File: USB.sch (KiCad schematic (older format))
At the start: 41 parts, among them J6 USB_A, J7 USB_B, U10 USB3320, U11 MIC2025-1YMM, U12 USB3320, U8 xc7z020clg400, Y1 Crystal, Y2 Crystal

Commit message: replacing rescue components foreal
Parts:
- U8: footprint Package_BGA:BGA-400_21.0x21.0mm_Layout20x20_P1.0mm -> DFTcustom:BGA400_0.8p_17mmx17mm
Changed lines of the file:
@@
 F 0 "U8" H 2050 3550 60  0000 L CNN
 F 1 "xc7z020clg400" H 2050 3450 60  0000 L CNN
-F 2 "Package_BGA:BGA-400_21.0x21.0mm_Layout20x20_P1.0mm" H 1850 3300 60  0001 C CNN
+F 2 "DFTcustom:BGA400_0.8p_17mmx17mm" H 1850 3300 60  0001 C CNN
 F 3 "" H 1850 3300 60  0001 C CNN
 	6    1850 3300

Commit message: still works, miraculously
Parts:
- C65, C66, C78, C83, C87: footprint Capacitors_SMD:C_0603 -> Capacitor_SMD:C_0603_1608Metric; symbol DFTBoard-rescue:C_Small- -> Device:C_Small
- C67, C73, C74: footprint Capacitors_SMD:C_1210 -> Capacitor_SMD:C_1210_3225Metric; symbol DFTBoard-rescue:C_Small- -> Device:C_Small
- C68, C70, C71, C72, C77, C79, C81, C82, C86: footprint Capacitors_SMD:C_0603 -> Capacitor_SMD:C_0603_1608Metric; symbol DFTBoard-rescue:C -> Device:C
- C69: footprint Capacitors_SMD:C_0402 -> Capacitor_SMD:C_0402_1005Metric; symbol DFTBoard-rescue:C -> Device:C
- C80: symbol DFTBoard-rescue:C -> Device:C
- R33, R36, R39: symbol DFTBoard-rescue:R -> Device:R
- R35: symbol DFTBoard-rescue:R_Small- -> Device:R_Small
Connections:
- net +1.8V renamed +1V8

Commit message: random updates
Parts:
- removed U8: xc7z020clg400, DFTcustom:BGA400_0.8p_17mmx17mm, symbol DFTBoard-rescue:xc7z020clg400-
- added U20: xc7z020clg484, DFTcustom:BGA-484_19.0x19.0mm_Layout22x22_P0.80mm_dia0.40mm, symbol xilinx7:xc7z020clg484
- C65, C66, C68, C70, C71, C72, C77, C78, C79, C81, C82, C83, C86, C87: footprint Capacitor_SMD:C_0603_1608Metric -> Capacitor_SMD:C_0402_1005Metric
- D3: footprint LEDs:LED_0603 -> Capacitor_SMD:C_0603_1608Metric
- R33, R35, R36, R39: footprint Resistors_SMD:R_0402 -> Resistor_SMD:R_0402_1005Metric
- U10, U12: footprint Microchip:32QFN-3304-5x5B -> Package_DFN_QFN:QFN-32-1EP_5x5mm_P0.5mm_EP3.1x3.1mm
- U11: footprint Crystal:Crystal_HC35-U -> SOP65P490X110-8N:SOP65P490X110-8N
- Y1, Y2: value Crystal -> ABM3-24.000MHZ-D2Y-T; footprint Crystal:Crystal_HC35-U -> ABM3-12.000MHZ-B2-T:XTAL500X320X130N
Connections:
- net +1V8: no longer C65.1, C66.1, C67.1, R33.2
- net +3V3: now also C65.1, C66.1, C67.1, R33.2, U20.A10 (VCCO_MIO1_501[4]), U20.B13 (VCCO_MIO1_501[4]), U20.D9 (VCCO_MIO1_501[4]), U20.E12 (VCCO_MIO1_501[4])
- net 1v35PG: now also U20.D7 (PS_MIO27_501)
- net SD_CD: now also U20.A13 (PS_MIO26_501)
- net SD_CMD: now also U20.E9 (PS_MIO17_501)
- net SD_D0: now also U20.A7 (PS_MIO18_501)
- net SD_D1: now also U20.E10 (PS_MIO19_501)
- net SD_D2: now also U20.A8 (PS_MIO20_501)
- net SD_D3: now also U20.F11 (PS_MIO21_501)
- net USB0_CLK: now also U20.A9 (PS_MIO36_501)
- net USB0_D0: now also U20.C7 (PS_MIO32_501)
- net USB0_D1: now also U20.G13 (PS_MIO33_501)
- net USB0_D2: now also U20.B12 (PS_MIO34_501)
- net USB0_D3: now also U20.F14 (PS_MIO35_501)
- net USB0_D4: now also U20.A12 (PS_MIO28_501)
- net USB0_D5: now also U20.B14 (PS_MIO37_501)
- net USB0_D6: now also U20.F13 (PS_MIO38_501)
- net USB0_D7: now also U20.C13 (PS_MIO39_501)
- net USB0_RST: now also U20.D10 (PS_MIO52_501)
- net USB0_dir: now also U20.E8 (PS_MIO29_501)
- net USB0_nxt: now also U20.F9 (PS_MIO31_501)
- net USB0_stp: now also U20.A11 (PS_MIO30_501)
- net USB1_CLK: now also U20.D11 (PS_MIO48_501)
- net USB1_D0: now also U20.E13 (PS_MIO44_501)
- net USB1_D1: now also U20.B9 (PS_MIO45_501)
- net USB1_D2: now also U20.D12 (PS_MIO46_501)
- net USB1_D3: now also U20.B10 (PS_MIO47_501)
- net USB1_D4: now also U20.E14 (PS_MIO40_501)
- net USB1_D5: now also U20.C14 (PS_MIO49_501)
- net USB1_D6: now also U20.D13 (PS_MIO50_501)
- net USB1_D7: now also U20.C10 (PS_MIO51_501)
- net USB1_RST: now also U20.C12 (PS_MIO53_501)
- net USB1_dir: now also U20.C8 (PS_MIO41_501)
- net USB1_nxt: now also U20.B11 (PS_MIO43_501)
- net USB1_stp: now also U20.D8 (PS_MIO42_501)
- net at R34.1: now also U20.D6 (PS_MIO16_501)
- net at R33.1: now also U20.C9 (PS_SRST_B_501)
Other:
- moved on the sheet: C68, C70, C71, C79, C81, C82

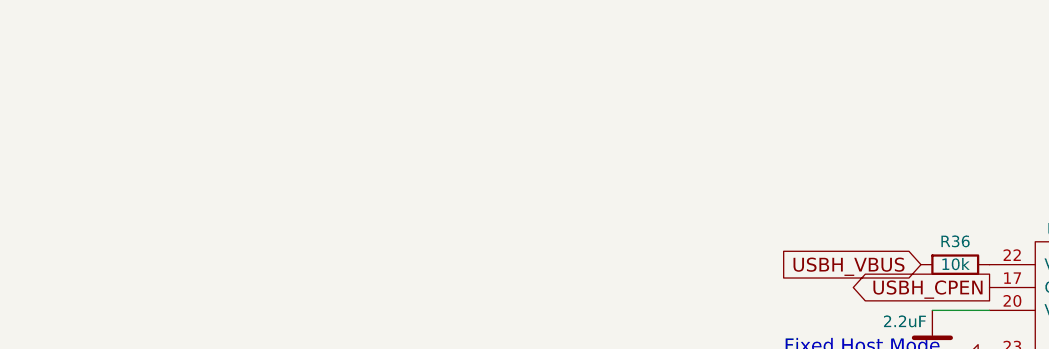
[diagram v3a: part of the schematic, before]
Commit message: everything placed, about to shrink text size globally
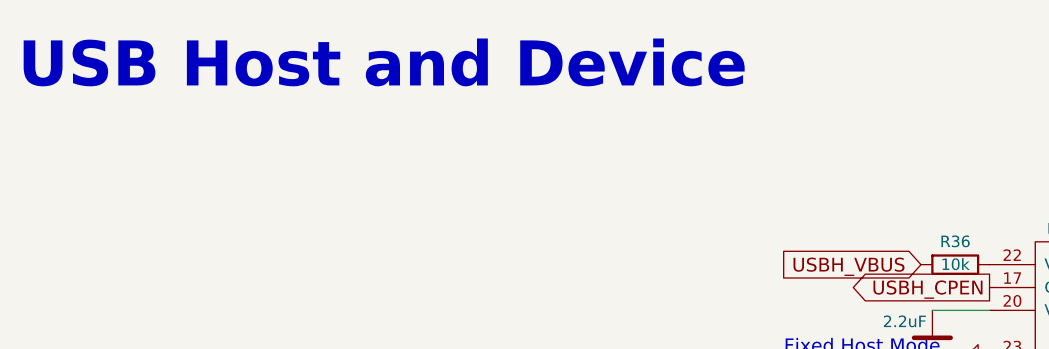
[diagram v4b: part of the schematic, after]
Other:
- note added: "USB Host and Device"
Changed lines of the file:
@@
 	1    0    0    -1
 $EndComp
+Text Notes 250  550  0    197  ~ 39
+USB Host and Device
 $EndSCHEMATC
